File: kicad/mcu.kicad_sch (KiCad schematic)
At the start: 42 parts, among them J8 USB_C_Receptacle_USB2.0_14P, J9 Conn_01x03, SW1 SW_Push, SW2 SW_Push, U12 ESP32-S3-WROOM-1-N8R2, U25 MCP23S17_SO

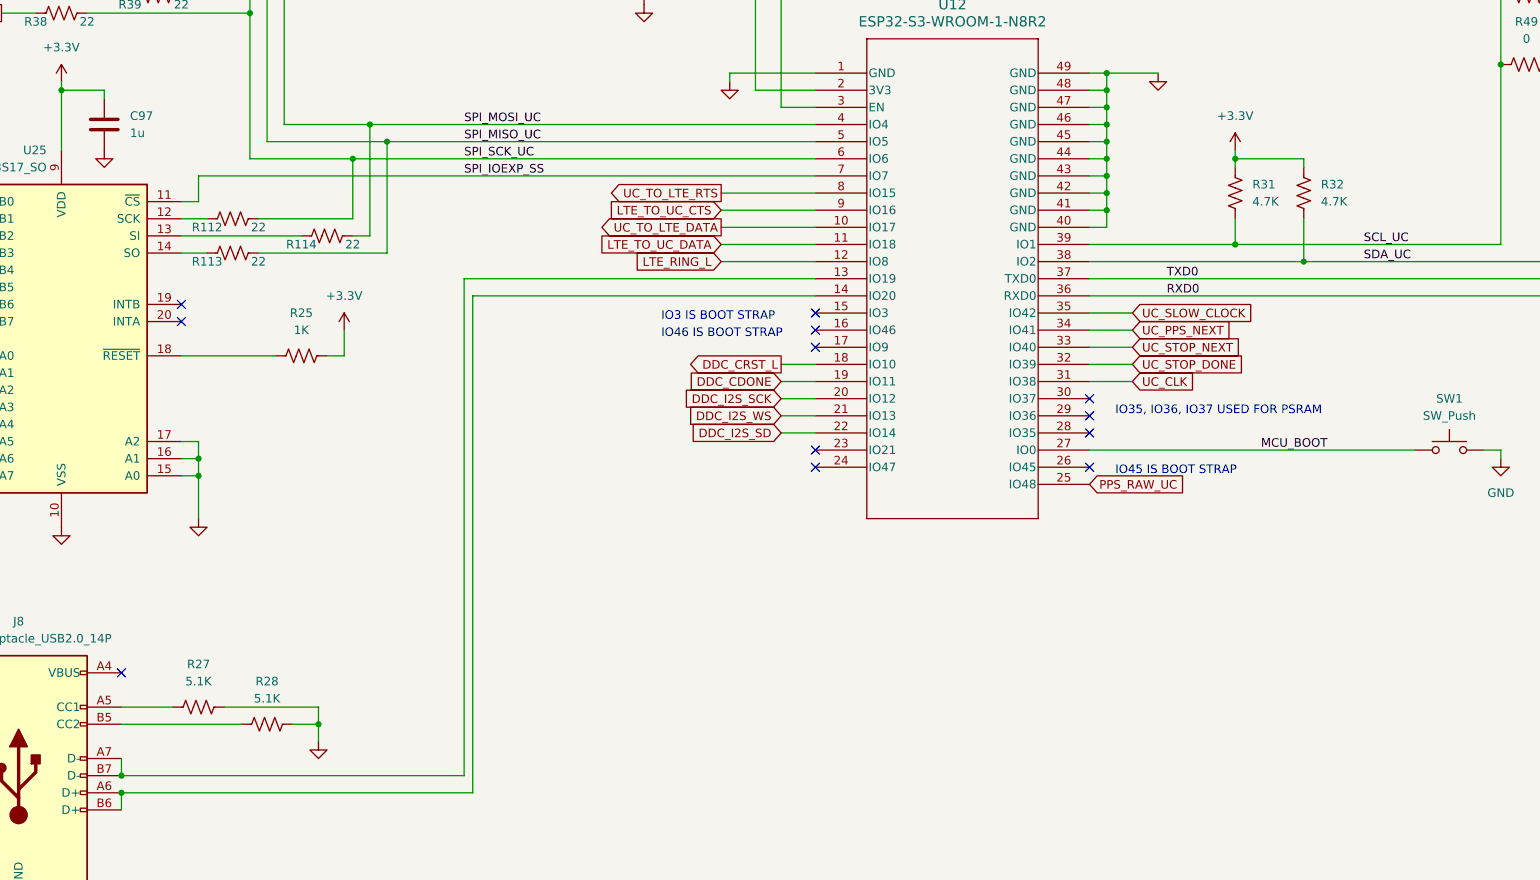
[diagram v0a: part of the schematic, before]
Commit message: add net names
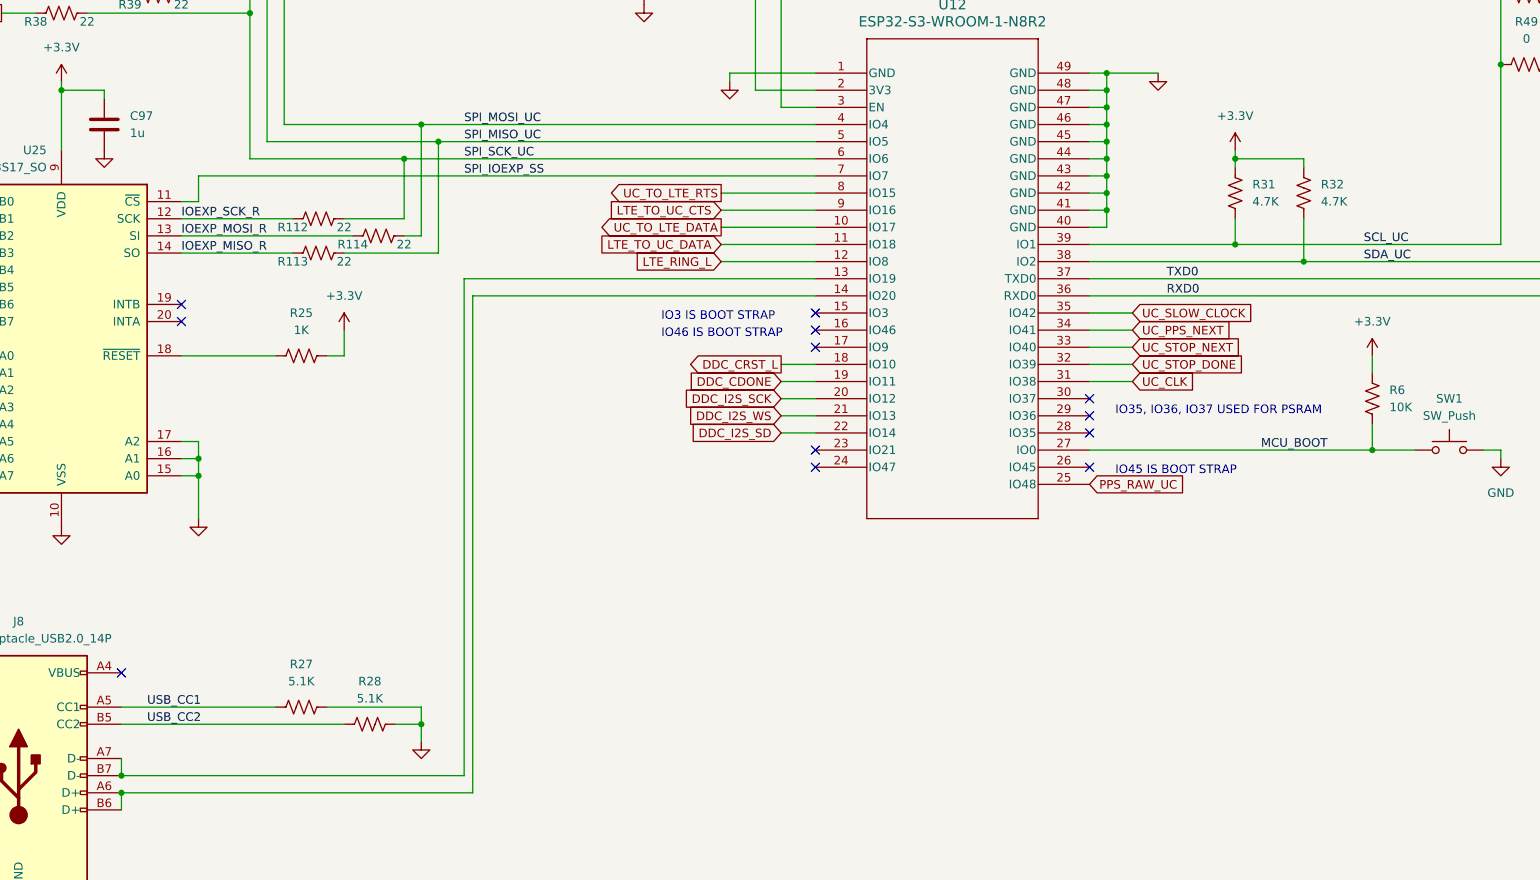
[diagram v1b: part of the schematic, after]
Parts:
- added R6: 10K, Resistor_SMD:R_0603_1608Metric_Pad0.98x0.95mm_HandSolder, symbol Device:R_US
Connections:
- net +3.3V: now also R6.1
- net MCU_BOOT: now also R6.2
- net IOEXP_SCK_R: now reaches R112.1, U25.12 (SCK)
- net USB_CC1: now reaches J8.A5 (CC1), R27.1
- net USB_CC2: now reaches J8.B5 (CC2), R28.1
- net IOEXP_MISO_R: now reaches R113.1, U25.14 (SO)
- net IOEXP_MOSI_R: now reaches R114.1, U25.13 (SI)
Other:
- moved on the sheet: R112, R113, R114, R27, R28

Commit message: start pcb
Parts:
- U25: value MCP23S17_SO -> MCP23S17_SS; footprint Package_SO:SOIC-28W_7.5x17.9mm_P1.27mm -> Package_SO:SSOP-28_5.3x10.2mm_P0.65mm; symbol Interface_Expansion:MCP23S17_SO -> Interface_Expansion:MCP23S17_SS
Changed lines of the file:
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@@
     )
   )
-  (symbol (lib_id "Interface_Expansion:MCP23S17_SO") (at 74.93 144.78 0) (mirror y) (unit 1)
+  (symbol (lib_id "Interface_Expansion:MCP23S17_SS") (at 74.93 144.78 0) (mirror y) (unit 1)
     (in_bom yes) (on_board yes) (dnp no)
     (property "Reference" "U25" (at 72.7359 116.84 0)
       (effects (font (size 1.27 1.27)) (justify left))
     )
-    (property "Value" "MCP23S17_SO" (at 72.7359 119.38 0)
-      (effects (font (size 1.27 1.27)) (justify left))
+    (property "Value" "MCP23S17_SS" (at 74.93 144.78 0)
+      (effects (font (size 1.27 1.27)))
     )
-    (property "Footprint" "Package_SO:SOIC-28W_7.5x17.9mm_P1.27mm" (at 69.85 170.18 0)
+    (property "Footprint" "Package_SO:SSOP-28_5.3x10.2mm_P0.65mm" (at 69.85 170.18 0)
       (effects (font (size 1.27 1.27)) (justify left) hide)
     )

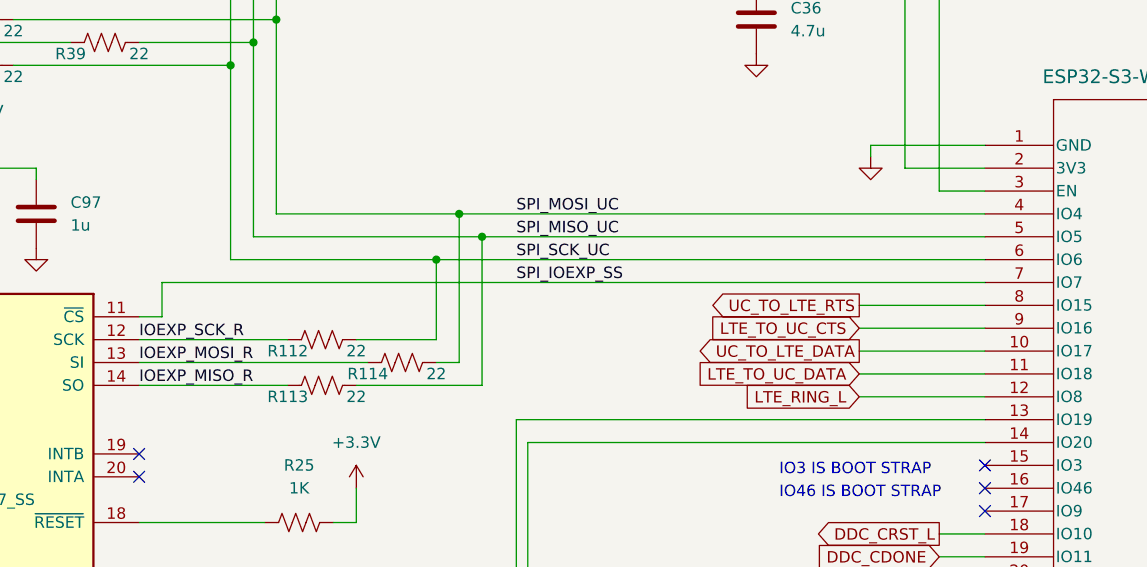
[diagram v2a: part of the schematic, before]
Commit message: add series term to ioexp_ss_r
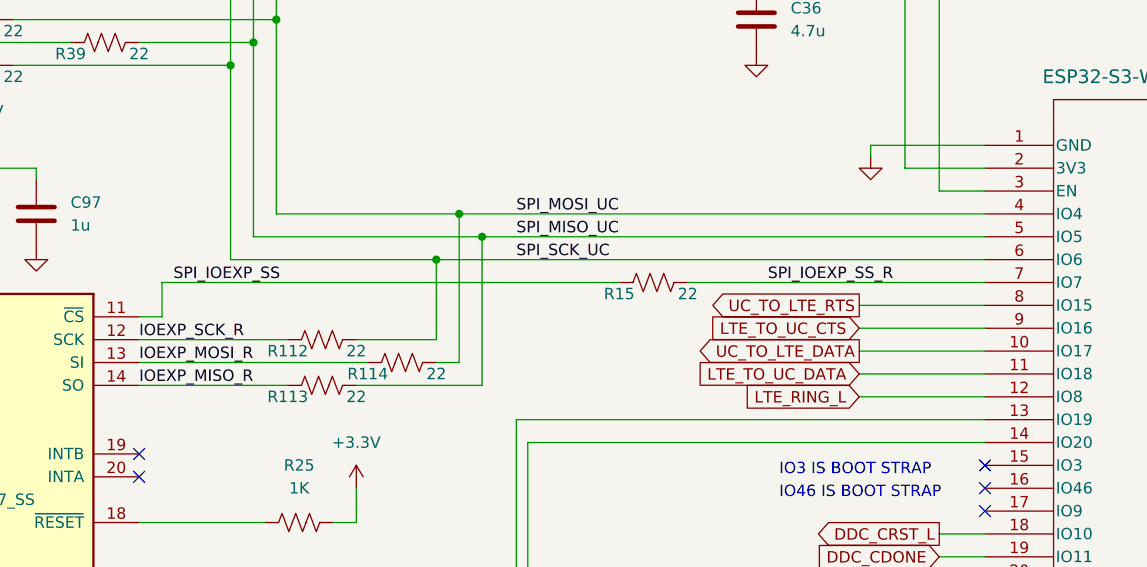
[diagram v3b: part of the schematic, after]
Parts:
- added R15: 22, Resistor_SMD:R_0603_1608Metric_Pad0.98x0.95mm_HandSolder, symbol Device:R_US
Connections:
- net SPI_IOEXP_SS: now also R15.1; no longer U12.7 (IO7)
- new net SPI_IOEXP_SS_R: R15.2, U12.7 (IO7)
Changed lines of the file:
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@@
     (stroke (width 0) (type default))
   )
-  (wire (pts (xy 186.69 120.65) (xy 95.25 120.65))
+  (wire (pts (xy 95.25 120.65) (xy 146.05 120.65))
     (stroke (width 0) (type default))
   )
@@
   )
   (wire (pts (xy 130.81 115.57) (xy 130.81 132.08))
+    (stroke (width 0) (type default))
+  )
+  (wire (pts (xy 153.67 120.65) (xy 186.69 120.65))
     (stroke (width 0) (type default))
   )
@@
     (effects (font (size 1.27 1.27)) (justify left bottom))
   )
+  (label "SPI_IOEXP_SS_R" (at 162.56 120.65 0) (fields_autoplaced)
+    (effects (font (size 1.27 1.27)) (justify left bottom))
+  )
   (label "MCU_RESET_L" (at 162.56 52.07 0) (fields_autoplaced)
     (effects (font (size 1.27 1.27)) (justify left bottom))
@@
     (effects (font (size 1.27 1.27)) (justify left bottom))
   )
-  (label "SPI_IOEXP_SS" (at 134.62 120.65 0) (fields_autoplaced)
+  (label "SPI_IOEXP_SS" (at 96.52 120.65 0) (fields_autoplaced)
     (effects (font (size 1.27 1.27)) (justify left bottom))
   )
@@
         )
       )
+    )
+  )
+  (symbol (lib_id "Device:R_US") (at 149.86 120.65 90) (unit 1)
+    (in_bom yes) (on_board yes) (dnp no)
+    (property "Reference" "R15" (at 146.05 121.92 90)
+      (effects (font (size 1.27 1.27)))
+    )
+    (property "Value" "22" (at 153.67 121.92 90)
+      (effects (font (size 1.27 1.27)))
+    )
+    (property "Footprint" "Resistor_SMD:R_0603_1608Metric_Pad0.98x0.95mm_HandSolder" (at 150.114 119.634 90)
+      (effects (font (size 1.27 1.27)) hide)
+    )
+    (property "Datasheet" "~" (at 149.86 120.65 0)
+      (effects (font (size 1.27 1.27)) hide)
+    )
+    (pin "1")
+    (pin "2")
+    (instances
+      (project "gpsrx"
+        (path "/c3c549bc-9d82-4b6a-bdb9-a3870905229d/cfc19a79-2a34-431b-9452-a8a8f8302b67"
+          (reference "R15") (unit 1)
+        )
+      )

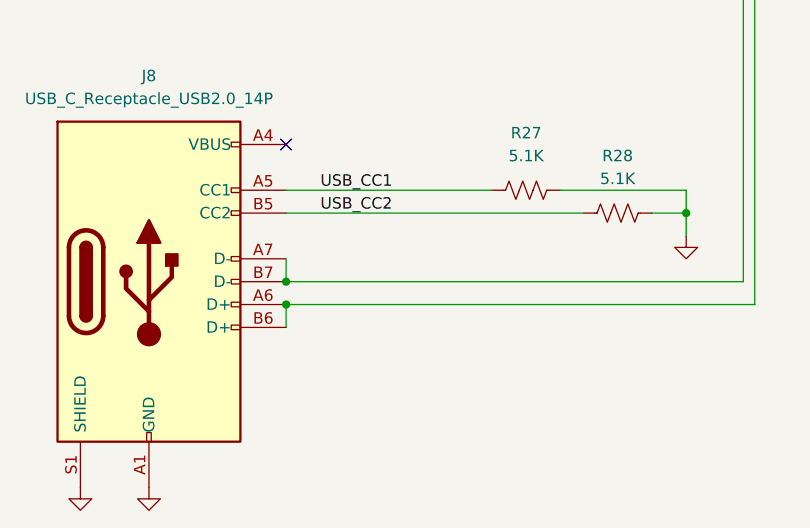
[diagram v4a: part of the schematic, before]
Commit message: fix schematic to align w/ pcb
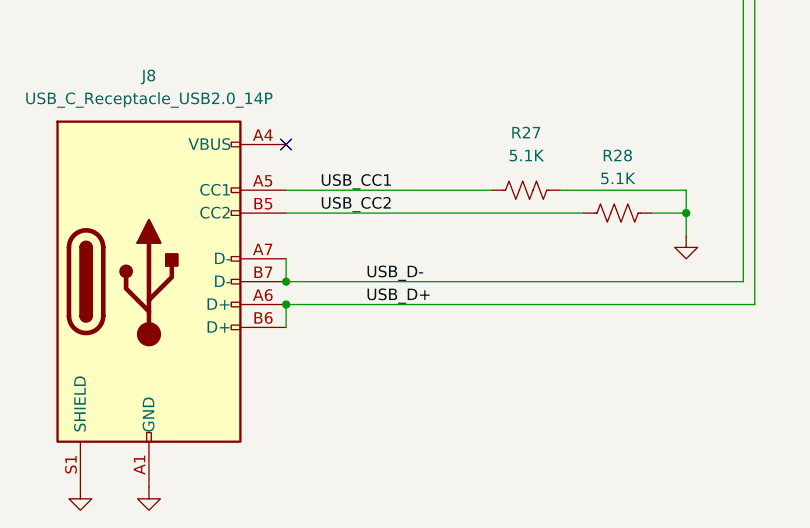
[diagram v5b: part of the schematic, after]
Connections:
- net USB_D-: now reaches J8.A7 (D-), J8.B7 (D-), U12.13 (IO19)
- net USB_D+: now reaches J8.A6 (D+), J8.B6 (D+), U12.14 (IO20)
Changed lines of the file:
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@@
+		)
+	)
+	(label "USB_D-"
+		(at 92.71 209.55 0)
+		(fields_autoplaced yes)
+		(effects
+			(font
+				(size 1.27 1.27)
+			)
+			(justify left bottom)
 		)
 	)
@@
 		(fields_autoplaced yes)
 		(effects
+			(font
+				(size 1.27 1.27)
+			)
+			(justify left bottom)
+		)
+	)
+	(label "USB_D+"
+		(at 92.71 212.09 0)
+		(fields_autoplaced yes)
+		(effects
